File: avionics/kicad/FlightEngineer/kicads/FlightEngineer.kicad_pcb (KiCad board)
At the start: 4 copper layers, 90 x 65 mm, 67 parts

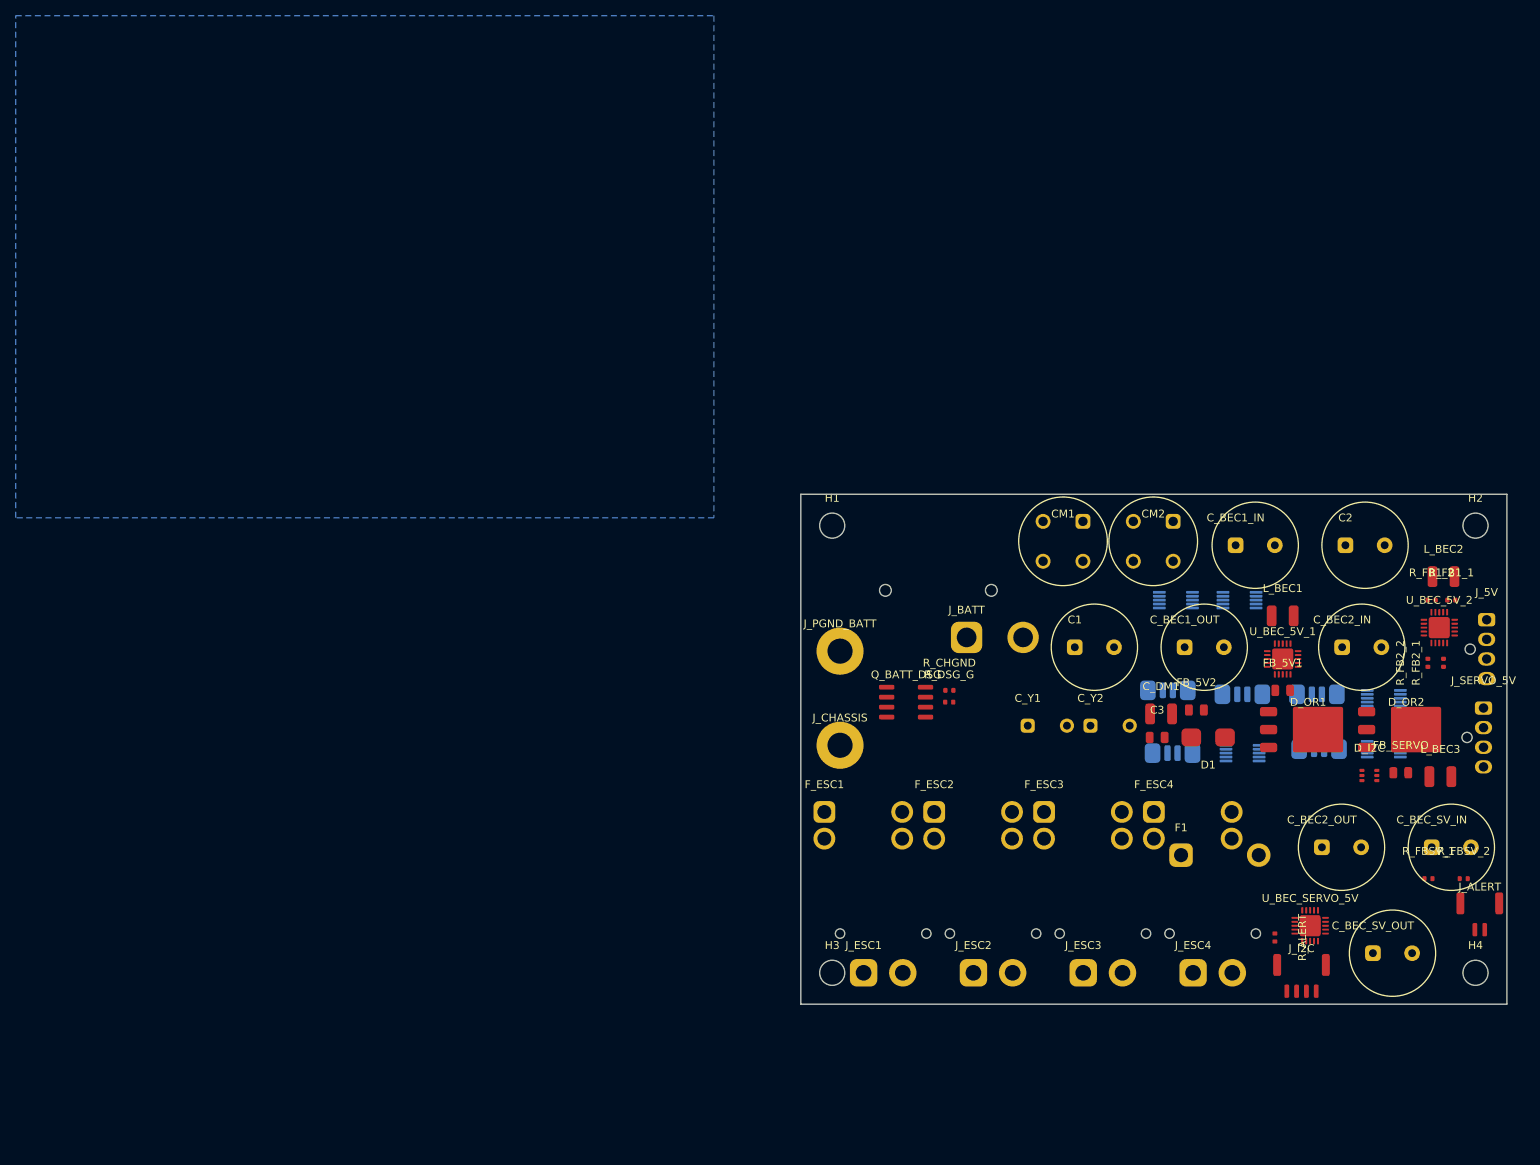
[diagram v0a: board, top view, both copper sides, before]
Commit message: feat(avionics): FlightEngineer schematic-first rebuild to ERC 0; PCB placed, DRC 31 open
Replaces FlightEngineer's legacy schematic/PCB (586 ERC violations, PCB pad
nets not matching the schematic at all, gen_flight_engineer.py itself confirmed
drifted per its own injector script's warning) with a fresh generator
pipeline matching Pilot/XO's method (gen_fe_sch.py / gen_fe_footprints.py /
gen_fe_pcb.py), transcribing every pin table from its own OEM datasheet.

Power path: TPS54620 x2 (dual-redundant diode-OR'd 5V BEC) + TPS54540 (6V
BEC), INA226 x5 (main bus + 4 ESC branches), BQ76930 6S cell monitor (Table
9-3 6-cell tap configuration). Trust module rebuilt to the CURRENT target per
FlightEngineer.md's own 2026-08-03 retarget note (MSPM0G3518-Q1 RHB-32 + real
SLB9672 + ISOW1044BDFMR + ISOW1412DFMR), not the superseded MSPM0G3507/
SLB9670 the old injector script still names; the RHB-32 pinmux is reused
verbatim from retarget_mspm0g351x_slb9672.py's own already-verified
FLIGHT_ENGINEER_REMAP/FLIGHT_ENGINEER_TPM_NETS tables rather than re-derived
from the 1500-line datasheet pin-attribute table. ISOW1412's EN/FLT pin is
now wired to a real MCU GPIO (RS485_FLT_N) instead of Pilot's hard-tied
convention, since the RHB-32 pinmux happened to free one.

One part-number defect found in FlightEngineer.md's own BOM and corrected
(flagged, not silently fixed): "AON6556" (Q_BATT_DSG, cited 60V/30A) does not
exist in AOSMD's catalog (their 30V AlphaMOS family tops out at AON6554/
6558; no 60V "6556" found) — substituted with AON6260, a real AOSMD 60V/85A
DFN5x6 MOSFET; NEEDS owner confirmation. MBRD1045CT and SMBJ33CA are
confirmed real via manufacturer/distributor catalog search but their
datasheet PDFs could not be fetched this pass (every mirror returned an HTML
block page) — standard package pinouts used, flagged for a follow-up fetch.

ERC 0 confirmed (kicad-cli sch erc --severity-all, 151 parts, 539 pins).

PCB: courtyard area was budgeted BEFORE layout per docs/solutions/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
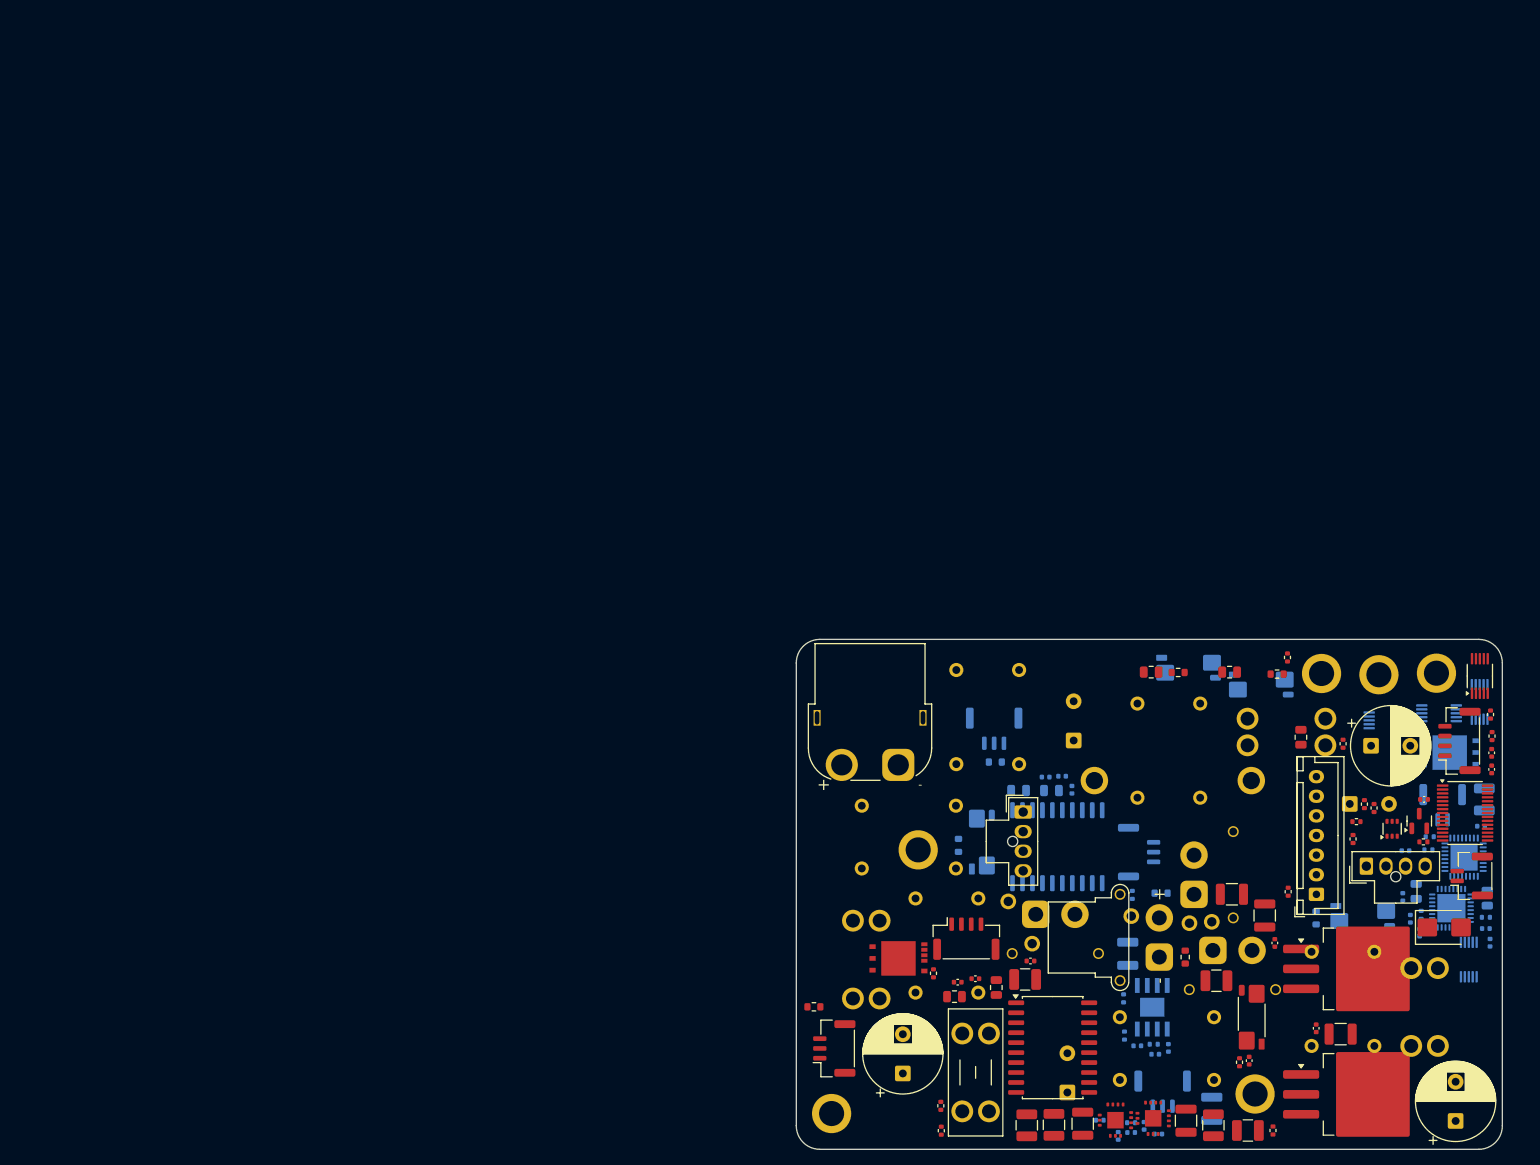
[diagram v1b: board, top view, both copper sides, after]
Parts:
- removed the C_BEC1_IN at (156.0, 68.0)
- removed C_BEC1_OUT, C_BEC2_OUT, C_BEC_SV_OUT: 100uF/50V, Capacitor_THT:CP_Radial_D10.0mm_P5.00mm
- removed the C_BEC2_IN at (169.6, 81.0)
- removed the C_BEC_SV_IN at (181.0, 106.5)
- removed FB_SERVO: WE-742792612, Capacitor_SMD:C_0805_2012Metric
- removed H1, H2, H3, H4: M3, MountingHole:MountingHole_3.2mm_M3
- removed the J_ALERT at (187.1, 115.0)
- removed the J_CHASSIS at (105.6, 93.5)
- removed the J_I2C at (164.4, 122.9)
- removed the J_PGND_BATT at (105.6, 81.5)
- removed J_SERVO_5V: NanoFit-4P_6V, Connector_Molex:Molex_Nano-Fit_105309-xx04_1x04_P2.50mm_Vertical
- removed L_BEC1, L_BEC2, L_BEC3: WE-744314100_10uH, Inductor_SMD:L_1210_3225Metric
- removed the Q_BATT_DSG at (114.0, 88.0)
- removed RS_1, RS_2, RS_3, RS_4: 1mOhm_Kelvin_2512, Flight Engineer:R_Shunt_CSS2H_2512K
- removed the RS_MAIN at (166.4, 87.0)
- removed R_FBSV_1: 100k, Resistor_SMD:R_0402_1005Metric
- removed R_FBSV_2: 30.1k, Resistor_SMD:R_0402_1005Metric
- removed U_BEC_SERVO_5V: TPS54620 sync buck 5.0V servo rail (pkg verify), Package_DFN_QFN:Texas_RGP0020D_VQFN-20-1EP_4x4mm_P0.5mm_EP2.7x2.7mm
- removed the U_IS_MAIN at (174.9, 87.5)
- added CM_ESC1: 7440640500, Serenity-Custom:Wurth_7440640500_CMC_THT, F.Cu at (147.2, 132.2)
- added CM_ESC2: 7440640500, Serenity-Custom:Wurth_7440640500_CMC_THT, B.Cu at (147.5, 94.2)
- added CM_ESC3: 7440640500, Serenity-Custom:Wurth_7440640500_CMC_THT, B.Cu at (169.7, 125.8)
- added CM_ESC4: 7440640500, Serenity-Custom:Wurth_7440640500_CMC_THT, B.Cu at (119.2, 119.0)
- added C_BEC1_BOOT: 100nF, Capacitor_SMD:C_0402_1005Metric, B.Cu at (144.3, 142.0)
- added C_BEC1_COMP: 2.2nF, Capacitor_SMD:C_0402_1005Metric, F.Cu at (157.7, 133.7)
- added C_BEC1_IN: 100uF 50V, Capacitor_SMD:C_1210_3225Metric, F.Cu at (149.7, 141.4)
- added C_BEC1_OUT1: 220uF, Capacitor_SMD:C_1210_3225Metric, F.Cu at (159.7, 115.2)
- added C_BEC1_OUT2: 100nF, Capacitor_SMD:C_0402_1005Metric, F.Cu at (161.0, 118.7)
- added C_BEC1_SS: 10nF, Capacitor_SMD:C_0402_1005Metric, B.Cu at (146.1, 143.1)
- added C_BEC2_BOOT: 100nF, Capacitor_SMD:C_0402_1005Metric, B.Cu at (138.7, 141.3)
- added C_BEC2_COMP: 2.2nF, Capacitor_SMD:C_0402_1005Metric, B.Cu at (142.7, 142.9)
- added C_BEC2_IN: 100uF 50V, Capacitor_SMD:C_1210_3225Metric, F.Cu at (136.5, 141.7)
- added C_BEC2_OUT1: 220uF, Capacitor_SMD:C_1210_3225Metric, F.Cu at (169.4, 130.3)
- added C_BEC2_OUT2: 100nF, Capacitor_SMD:C_0402_1005Metric, F.Cu at (166.3, 129.6)
- added C_BEC2_SS: 10nF, Capacitor_SMD:C_0402_1005Metric, B.Cu at (141.0, 143.3)
- added C_BEC6_BOOT: 100nF, Capacitor_SMD:C_0402_1005Metric, B.Cu at (147.4, 132.1)
- added C_BEC6_COMP: 1nF, Capacitor_SMD:C_0402_1005Metric, B.Cu at (143.5, 131.8)
- added C_BEC_SV_IN: 100uF 50V, Capacitor_SMD:C_1210_3225Metric, B.Cu at (142.2, 120.1)
- added C_BEC_SV_OUT1: 100uF, Capacitor_SMD:C_1210_3225Metric, B.Cu at (153.0, 139.8)
- added C_BEC_SV_OUT2: 100nF, Capacitor_SMD:C_0402_1005Metric, B.Cu at (145.8, 132.9)
- added C_CAP1: 0.1uF, Capacitor_SMD:C_0402_1005Metric, F.Cu at (188.6, 96.6)
- added C_CAP2: 0.1uF, Capacitor_SMD:C_0402_1005Metric, F.Cu at (180.0, 100.4)
- added C_DEC1: 470uF 35V low-ESR, Capacitor_THT:CP_Radial_D10.0mm_P5.00mm, B.Cu at (134.6, 137.8)
- added C_DEC2: 470uF 35V low-ESR, Capacitor_THT:CP_Radial_D10.0mm_P5.00mm, B.Cu at (135.4, 92.9)
- added C_DEC3: 470uF 35V low-ESR, Capacitor_THT:CP_Radial_D10.0mm_P5.00mm, F.Cu at (184.0, 141.4)
- added C_DEC4: 470uF 35V low-ESR, Capacitor_THT:CP_Radial_D10.0mm_P5.00mm, F.Cu at (113.6, 135.3)
- added C_H_IN: 10uF, Capacitor_SMD:C_0805_2012Metric, B.Cu at (188.1, 113.0)
- added C_H_OUT: 22uF, Capacitor_SMD:C_0805_2012Metric, B.Cu at (179.0, 112.1)
- added C_ISOCAN1: 10nF, Capacitor_SMD:C_0402_1005Metric, B.Cu at (135.1, 99.2)
- added C_ISOCAN2: 10uF, Capacitor_SMD:C_0805_2012Metric, B.Cu at (132.5, 99.3)
- added C_ISOCAN3: 100nF, Capacitor_SMD:C_0402_1005Metric, B.Cu at (131.8, 97.6)
- added C_ISOCAN4: 10nF, Capacitor_SMD:C_0402_1005Metric, B.Cu at (133.9, 97.4)
- added C_ISOCAN5: 10uF, Capacitor_SMD:C_0805_2012Metric, B.Cu at (128.3, 99.3)
- added C_MCU_3V3: 100nF, Capacitor_SMD:C_0402_1005Metric, B.Cu at (187.3, 103.8)
- added C_MCU_VCORE: 1uF, Capacitor_SMD:C_0402_1005Metric, B.Cu at (177.3, 112.8)
- added C_NTC: 100nF X7R, Capacitor_SMD:C_0402_1005Metric, B.Cu at (177.7, 106.9)
- added C_REGOUT: 1uF, Capacitor_SMD:C_0402_1005Metric, F.Cu at (188.6, 94.5)
- added C_RS485_1: 10nF, Capacitor_SMD:C_0402_1005Metric, F.Cu at (129.8, 121.0)
- added C_RS485_2: 10uF, Capacitor_SMD:C_0805_2012Metric, F.Cu at (125.5, 124.4)
- added C_RS485_3: 100nF, Capacitor_SMD:C_0402_1005Metric, F.Cu at (122.8, 123.3)
- added C_RS485_4: 10nF, Capacitor_SMD:C_0402_1005Metric, F.Cu at (120.6, 123.7)
- added C_RS485_5: 10uF, Capacitor_SMD:C_0805_2012Metric, F.Cu at (120.2, 125.5)
- added C_TPM1: 1uF, Capacitor_SMD:C_0402_1005Metric, B.Cu at (187.9, 116.9)
- added C_TPM2: 100nF, Capacitor_SMD:C_0402_1005Metric, B.Cu at (179.5, 117.4)
- added C_TPM3: 100nF, Capacitor_SMD:C_0402_1005Metric, B.Cu at (178.3, 115.6)
- added C_TPM4: 100nF, Capacitor_SMD:C_0402_1005Metric, B.Cu at (188.4, 118.7)
- added ESC1_LINK: 0R link, Resistor_SMD:R_0603_1608Metric, F.Cu at (149.6, 120.5)
- added ESC2_LINK: 0R link, Resistor_SMD:R_0603_1608Metric, B.Cu at (146.5, 112.3)
- added ESC3_LINK: 0R link, Resistor_SMD:R_0603_1608Metric, B.Cu at (166.3, 115.5)
- added ESC4_LINK: 0R link, Resistor_SMD:R_0603_1608Metric, B.Cu at (120.7, 106.3)
- added FB_6V: 742792612, Inductor_SMD:L_1210_3225Metric, F.Cu at (129.2, 123.4)
- added J_485_IN: SM03B-GHS-TB, Connector_JST:JST_GH_SM03B-GHS-TB_1x03-1MP_P1.25mm_Horizontal, B.Cu at (146.7, 137.7)
- added J_485_OUT: SM03B-GHS-TB, Connector_JST:JST_GH_SM03B-GHS-TB_1x03-1MP_P1.25mm_Horizontal, F.Cu at (104.8, 132.1)
- added J_6V: Nano-Fit 4P, Connector_Molex:Molex_Nano-Fit_105309-xx04_1x04_P2.50mm_Vertical, F.Cu at (172.7, 108.9)
- added J_ALERT: SM02B-GHS-TB, Connector_JST:JST_GH_SM02B-GHS-TB_1x02-1MP_P1.25mm_Horizontal, F.Cu at (186.1, 110.2)
- added J_BAL: XH-7P, Connector_JST:JST_XH_B7B-XH-A_1x07_P2.50mm_Vertical, F.Cu at (166.3, 112.5)
- added J_CAN_IN: SM03B-GHS-TB, Connector_JST:JST_GH_SM03B-GHS-TB_1x03-1MP_P1.25mm_Horizontal, B.Cu at (143.7, 107.1)
- added J_CAN_OUT: SM03B-GHS-TB, Connector_JST:JST_GH_SM03B-GHS-TB_1x03-1MP_P1.25mm_Horizontal, B.Cu at (125.2, 91.4)
- added J_CHASSIS: M3 standoff x4, Serenity-Custom:M3_Chassis_Lug_PGND, F.Cu at (167.0, 84.3)
- added J_I2C: SM04B-GHS-TB, Connector_JST:JST_GH_SM04B-GHS-TB_1x04-1MP_P1.25mm_Horizontal, F.Cu at (184.5, 92.9)
- added J_NTC: SM02B-GHS-TB, Connector_JST:JST_GH_SM02B-GHS-TB_1x02-1MP_P1.25mm_Horizontal, B.Cu at (182.4, 101.1)
- added J_PGND_BATT: M3 chassis lug, Serenity-Custom:M3_Chassis_Lug_PGND, F.Cu at (174.3, 84.5)
- added J_SHLD_5V: PGND via, Serenity-Custom:PGND_ViaPad_1p2mm, F.Cu at (150.1, 116.2)
- added J_SHLD_6V: PGND via, Serenity-Custom:PGND_ViaPad_1p2mm, F.Cu at (153.0, 116.0)
- added J_SHLD_ALERT: PGND via, Serenity-Custom:PGND_ViaPad_1p2mm, B.Cu at (142.7, 115.3)
- added J_SHLD_ESC1: M3 chassis lug, Serenity-Custom:M3_Chassis_Lug_PGND, F.Cu at (181.6, 84.3)
- added J_SHLD_ESC2: M3 chassis lug, Serenity-Custom:M3_Chassis_Lug_PGND, F.Cu at (104.5, 140.4)
- added J_SHLD_ESC3: M3 chassis lug, Serenity-Custom:M3_Chassis_Lug_PGND, B.Cu at (158.5, 137.9)
- added J_SHLD_ESC4: M3 chassis lug, Serenity-Custom:M3_Chassis_Lug_PGND, B.Cu at (115.5, 106.8)
- added J_SHLD_I2C: PGND via, Serenity-Custom:PGND_ViaPad_1p2mm, F.Cu at (130.1, 118.8)
- added J_SHLD_NTC: PGND via, Serenity-Custom:PGND_ViaPad_1p2mm, F.Cu at (127.0, 113.4)
- added J_SWD_H: SM04B-GHS-TB, Connector_JST:JST_GH_SM04B-GHS-TB_1x04-1MP_P1.25mm_Horizontal, F.Cu at (121.7, 118.2)
- added L1: 10uH 6A, Inductor_SMD:L_1210_3225Metric, F.Cu at (157.6, 142.6)
- added L2: 10uH 6A, Inductor_SMD:L_1210_3225Metric, F.Cu at (129.4, 141.9)
- added L3: 10uH 6A, Inductor_SMD:L_1210_3225Metric, F.Cu at (153.6, 123.5)
- added L_H1: 2.2uH, Inductor_SMD:L_1210_3225Metric, B.Cu at (187.7, 100.4)
- added Q_BATT_CHG: AON6260 (DNP), Serenity-Custom:AOSMD_DFN5x6-8L, B.Cu at (183.3, 94.4)
- added Q_BATT_DSG: AON6260, Serenity-Custom:AOSMD_DFN5x6-8L, F.Cu at (113.0, 120.7)
- added RS1: 1mOhm 3W Kelvin, Resistor_SMD:R_Shunt_Vishay_WSK2512_6332Metric_T1.19mm, F.Cu at (158.0, 128.2)
- added RS2: 1mOhm 3W Kelvin, Resistor_SMD:R_Shunt_Vishay_WSK2512_6332Metric_T1.19mm, B.Cu at (150.0, 83.6)
- added RS3: 1mOhm 3W Kelvin, Resistor_SMD:R_Shunt_Vishay_WSK2512_6332Metric_T1.19mm, B.Cu at (172.2, 115.3)
- added RS4: 1mOhm 3W Kelvin, Resistor_SMD:R_Shunt_Vishay_WSK2512_6332Metric_T1.19mm, B.Cu at (123.7, 105.8)
- added RS_MAIN: 1mOhm 5W Kelvin, Resistor_SMD:R_Shunt_Vishay_WSK2512_6332Metric_T1.19mm, B.Cu at (159.3, 85.8)
- added R_485TERM: 120R, Resistor_SMD:R_0603_1608Metric, F.Cu at (102.2, 126.8)
- added R_BAL1: 100R, Resistor_SMD:R_0402_1005Metric, F.Cu at (162.7, 112.2)
- added R_BAL2: 100R, Resistor_SMD:R_0402_1005Metric, F.Cu at (171.0, 105.4)
- added R_BAL3: 100R, Resistor_SMD:R_0402_1005Metric, F.Cu at (171.4, 103.2)
- added R_BAL4: 100R, Resistor_SMD:R_0402_1005Metric, F.Cu at (172.4, 101.0)
- added R_BAL5: 100R, Resistor_SMD:R_0402_1005Metric, F.Cu at (173.7, 101.5)
- added R_BAL6: 100R, Resistor_SMD:R_0402_1005Metric, F.Cu at (169.7, 93.3)
- added R_CANSTB: 0R, Resistor_SMD:R_0402_1005Metric, B.Cu at (142.8, 112.6)
- added R_CANTERM: 120R, Resistor_SMD:R_0603_1608Metric, B.Cu at (125.4, 95.6)
- added R_EN_BIAS: 100k, Resistor_SMD:R_0402_1005Metric, B.Cu at (145.6, 131.6)
- added R_FB6_1: 64.9k 1%, Resistor_SMD:R_0402_1005Metric, B.Cu at (141.7, 125.8)
- added R_FB6_2: 10.0k 1%, Resistor_SMD:R_0402_1005Metric, B.Cu at (141.8, 130.5)
- added R_GND_PGND: 0R, Resistor_SMD:R_0603_1608Metric, F.Cu at (148.7, 84.2)
- added R_I2C_SCL: 4.7k, Resistor_SMD:R_0402_1005Metric, F.Cu at (188.7, 92.3)
- added R_I2C_SDA: 4.7k, Resistor_SMD:R_0402_1005Metric, F.Cu at (188.5, 89.6)
- added R_MCU_NRST: 10k, Resistor_SMD:R_0402_1005Metric, B.Cu at (180.6, 106.8)
- added R_NTC_PU: 10k, Resistor_SMD:R_0402_1005Metric, B.Cu at (180.7, 105.2)
- added R_RS485FLT_PU: 10k, Resistor_SMD:R_0402_1005Metric, F.Cu at (118.4, 139.5)
- added R_TPM10: 10k, Resistor_SMD:R_0402_1005Metric, B.Cu at (179.7, 115.1)
- added R_TPMCS: 10k, Resistor_SMD:R_0402_1005Metric, B.Cu at (187.9, 115.4)
- added U_BEC_6V: TPS54540DDAR, Package_SO:TI_SO-PowerPAD-8, B.Cu at (145.4, 126.9)
- added U_CELL: BQ76930PWRQ1, Package_SO:TSSOP-30_4.4x7.8mm_P0.5mm, F.Cu at (185.3, 102.1)
- added U_ISOCAN: ISOW1044BDFMR, Package_SO:SOIC-20W_7.5x12.8mm_P1.27mm, B.Cu at (133.3, 106.4)
- added U_IS_MAIN: INA226AIDGSR, Package_SO:VSSOP-10_3x3mm_P0.5mm, B.Cu at (185.7, 120.8)
- added U_MCU: MSPM0G3518-Q1, Package_DFN_QFN:Texas_RHB0032E_VQFN-32-1EP_5x5mm_P0.5mm_EP3.45x3.45mm, B.Cu at (185.1, 107.8)
- added U_REG_3V3_H: TLV62569DBVR, Package_TO_SOT_SMD:SOT-23, F.Cu at (179.4, 103.2)
- added U_RS485: ISOW1412DFMR, Package_SO:SOIC-20W_7.5x12.8mm_P1.27mm, F.Cu at (132.7, 132.0)
- added U_TPM: SLB9672XU20, Package_DFN_QFN:QFN-32-1EP_5x5mm_P0.5mm_EP3.6x3.6mm, B.Cu at (183.5, 114.3)
- added VDIS_LINK: 0R link, Resistor_SMD:R_0603_1608Metric, F.Cu at (161.3, 84.4)
- C1: value 220uF/35V -> 220uF 35V; moved to B.Cu
- C2: value 220uF/35V -> 220uF 35V
- C3: value 100nF/50V -> 100nF X7R 0805
- CM1, CM2: value WE-SL5_7440640500 -> 7440640500; footprint Flight Engineer:CMC_WE-SL5_7440640500 -> Serenity-Custom:Wurth_7440640500_CMC_THT
- C_DM1: value 10uF/50V -> 10uF 50V X7R 1210; footprint Inductor_SMD:L_1210_3225Metric -> Capacitor_SMD:C_1210_3225Metric
- C_Y1, C_Y2: value 4.7nF/250V_Y2 -> 4.7nF 250V Y2; footprint Capacitor_THT:C_Disc_D4.3mm_W1.9mm_P5.00mm -> Capacitor_SMD:C_0805_2012Metric
- D_OR1, D_OR2: footprint Package_TO_SOT_SMD:TO-252-3_TabPin2 -> Package_TO_SOT_SMD:TO-263-3_TabPin2
- F1: value FuseHolder_MAXI_150A -> 0297150.ZXNV 150A MAXI; footprint Flight Engineer:FuseHolder_MAXI_PCB -> Serenity-Custom:MAXI_Blade_Fuseholder_2P
- FB_5V1, FB_5V2: value WE-742792612 -> 742792612; footprint Capacitor_SMD:C_0805_2012Metric -> Inductor_SMD:L_1210_3225Metric
- F_ESC1: value FuseHolder_Mini_40A -> 0297040.WXNV 40A mini
- F_ESC2, F_ESC3, F_ESC4: value FuseHolder_Mini_40A -> 0297040.WXNV 40A mini; moved to B.Cu
- J_5V: value NanoFit-4P_5V -> Nano-Fit 4P
- J_ESC1: value XT30PW-F_ESC1 -> XT30PW-F
- J_ESC2: value XT30PW-F_ESC2 -> XT30PW-F; moved to B.Cu
- J_ESC3: value XT30PW-F_ESC3 -> XT30PW-F; moved to B.Cu
- J_ESC4: value XT30PW-F_ESC4 -> XT30PW-F; moved to B.Cu
- R_CHGND: value 0R -> 0R socketed
- R_FB1_1, R_FB2_1: value 100k -> 56.2k 1%
- R_FB1_2: value 22.1k -> 10.0k 1%
- R_FB2_2: value 22.1k -> 10.0k 1%; moved to B.Cu
- U_BEC_5V_1, U_BEC_5V_2: footprint Package_DFN_QFN:Texas_RGP0020D_VQFN-20-1EP_4x4mm_P0.5mm_EP2.7x2.7mm -> Serenity-Custom:Texas_RGY0014A_VQFN-14-1EP_3.5x3.5mm
- U_IS1: value INA226_0x40 -> INA226AIDGSR; footprint Package_SO:MSOP-10_3x3mm_P0.5mm -> Package_SO:VSSOP-10_3x3mm_P0.5mm; moved to F.Cu
- U_IS2: value INA226_0x41 -> INA226AIDGSR; footprint Package_SO:MSOP-10_3x3mm_P0.5mm -> Package_SO:VSSOP-10_3x3mm_P0.5mm
- U_IS3: value INA226_0x42 -> INA226AIDGSR; footprint Package_SO:MSOP-10_3x3mm_P0.5mm -> Package_SO:VSSOP-10_3x3mm_P0.5mm
- U_IS4: value INA226_0x43 -> INA226AIDGSR; footprint Package_SO:MSOP-10_3x3mm_P0.5mm -> Package_SO:VSSOP-10_3x3mm_P0.5mm
- moved R_FB2_1 87.5 mm to (118.5, 142.6)
- moved U_BEC_5V_2 75.1 mm to (140.7, 141.3)
- moved R_FB1_1 71.3 mm to (160.8, 142.6), turned to 90 degrees
- moved R_FB2_2 69.8 mm to (142.7, 141.6), turned to 0 degrees
- moved J_5V 64.0 mm to (128.9, 102.0)
- moved R_FB1_2 63.8 mm to (156.5, 133.9), turned to 90 degrees
- moved U_BEC_5V_1 60.8 mm to (145.5, 141.1)
- moved F_ESC3 58.4 mm to (181.8, 131.8), turned to 90 degrees
- moved FB_5V1 56.1 mm to (153.2, 141.9), turned to 90 degrees
- moved FB_5V2 55.9 mm to (132.8, 141.9), turned to 90 degrees
- moved D_OR2 46.9 mm to (172.0, 138.0)
- moved R_CHGND 43.3 mm to (162.6, 82.3), turned to 90 degrees
- moved CM1 42.5 mm to (114.4, 105.2)
- moved F_ESC4 42.3 mm to (110.6, 125.8), turned to 90 degrees
- moved F_ESC1 42.0 mm to (121.2, 140.2), turned to 90 degrees
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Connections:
- C1 pad 1: VDIS -> VBAT_F1
- C2 pad 1: VDIS -> VBAT_F1
- C3 pad 1: VDIS -> VBAT_F1
- CM1 pad 1: VDIS -> BATT_RAW_P
- CM1 pad 2: VDIS -> BATT_CM1_P
- CM1 pad 3: PGND -> BATT_RAW_N
- CM1 pad 4: PGND -> BATT_CM1_N
- CM2 pad 1: VDIS -> BATT_CM1_P
- CM2 pad 2: VDIS -> VBAT
- CM2 pad 3: PGND -> BATT_CM1_N
- C_DM1 pad 1: VDIS -> VBAT_F1
- C_Y1 pad 1: VDIS -> VBAT_F1
- C_Y1 pad 2: CHASSIS -> J_CHASSIS_NET
- C_Y2 pad 2: CHASSIS -> J_CHASSIS_NET
- D1 pad 1: PGND -> VBAT_F1
- D1 pad 2: VDIS -> PGND
- D_I2C pad 1: PGND -> I2C_SCL
- D_I2C pad 2: PDB_SDA_RAW -> PGND
- D_I2C pad 3: PDB_SCL_RAW -> I2C_SDA
- D_I2C pad 4: PDB_SCL -> (no net)
- D_I2C pad 5: PDB_SDA -> +5V
- D_I2C pad 6: +5V -> (no net)
- D_OR1 pad 1: BEC1_PRE_OR -> +5V_PRE_OR1
- D_OR1 pad 2: +5V -> +5V_AVIONICS
- D_OR1 pad 3: BEC2_PRE_OR -> +5V_AVIONICS
- D_OR2 pad 1: BEC2_PRE_OR -> +5V_PRE_OR2
- D_OR2 pad 2: +5V -> +5V_AVIONICS
- D_OR2 pad 3: BEC2_PRE_OR -> +5V_AVIONICS
- F1 pad 1: VDIS -> VBAT
- F1 pad 2: VDIS -> VBAT_F1
- FB_5V1 pad 2: BEC1_VIN_F -> VDIS_5V1
- FB_5V2 pad 2: BEC2_VIN_F -> VDIS_5V2
- F_ESC1 pad 1: VBAT -> VDIS
- F_ESC2 pad 1: VBAT -> VDIS
- F_ESC3 pad 1: VBAT -> VDIS
- F_ESC4 pad 1: VBAT -> VDIS
- J_5V pad 1: PGND -> +5V_AVIONICS
- J_5V pad 2: PGND -> +5V_AVIONICS
- J_5V pad 3: +5V -> GND
- J_5V pad 4: +5V -> GND
- J_BATT pad 1: VDIS -> BATT_RAW_P
- J_BATT pad 2: PGND -> BATT_RAW_N
- J_ESC1 pad 1: ESC1_RS_OUT -> ESC1_OUT
- J_ESC2 pad 1: ESC2_RS_OUT -> ESC2_OUT
- J_ESC3 pad 1: ESC3_RS_OUT -> ESC3_OUT
- J_ESC4 pad 1: ESC4_RS_OUT -> ESC4_OUT
- R_ALERT pad 2: PDB_ALERT_N -> CELL_ALERT_N
- R_CHGND pad 1: PGND -> J_CHASSIS_NET
- R_CHGND pad 2: CHASSIS -> PGND
- R_DSG_G pad 1: DSG_GATE -> BATT_DSG_GATE
- R_DSG_G pad 2: PGND -> BATT_DSG_GATE_R
- R_FB1_1 pad 1: BEC1_PRE_OR -> +5V_PRE_OR1
- R_FB1_2 pad 2: PGND -> GND
- R_FB2_1 pad 1: BEC2_PRE_OR -> +5V_PRE_OR2
- R_FB2_2 pad 2: PGND -> GND
- U_BEC_5V_1 pad 1: BEC1_VIN_F -> GND
- U_BEC_5V_1 pad 10: PGND -> +3V3_BIAS_EN
- U_BEC_5V_1 pad 11: BEC1_PRE_OR -> BEC1_SW
- U_BEC_5V_1 pad 12: (no net) -> BEC1_SW
- U_BEC_5V_1 pad 13: (no net) -> BEC1_BOOT
- U_BEC_5V_1 pad 15: BEC1_VIN_F -> GND
- U_BEC_5V_1 pad 2: (no net) -> GND
- U_BEC_5V_1 pad 3: (no net) -> GND
- U_BEC_5V_1 pad 4: (no net) -> VDIS
- U_BEC_5V_1 pad 5: BEC1_SW -> VDIS
- U_BEC_5V_1 pad 6: BEC1_SW -> VDIS
- U_BEC_5V_1 pad 7: PGND -> BEC1_FB
- U_BEC_5V_1 pad 8: PGND -> BEC1_COMP
- U_BEC_5V_1 pad 9: PGND -> BEC1_SS
- U_BEC_5V_2 pad 1: BEC2_VIN_F -> GND
- U_BEC_5V_2 pad 10: PGND -> +3V3_BIAS_EN
- U_BEC_5V_2 pad 11: BEC2_PRE_OR -> BEC2_SW
- U_BEC_5V_2 pad 12: (no net) -> BEC2_SW
- U_BEC_5V_2 pad 13: (no net) -> BEC2_BOOT
- U_BEC_5V_2 pad 15: BEC2_VIN_F -> GND
- U_BEC_5V_2 pad 2: (no net) -> GND
- U_BEC_5V_2 pad 3: (no net) -> GND
- U_BEC_5V_2 pad 4: (no net) -> VDIS
- U_BEC_5V_2 pad 5: BEC2_SW -> VDIS
- U_BEC_5V_2 pad 6: BEC2_SW -> VDIS
- U_BEC_5V_2 pad 7: PGND -> BEC2_FB
- U_BEC_5V_2 pad 8: PGND -> BEC2_COMP
- U_BEC_5V_2 pad 9: PGND -> BEC2_SS
- U_IS1 pad 1: ESC1_SNS_P -> GND
- U_IS1 pad 10: ESC1_FUSED -> SHUNT1_P
- U_IS1 pad 2: ESC1_SNS_N -> GND
- U_IS1 pad 3: PGND -> (no net)
- U_IS1 pad 4: +5V -> I2C_SDA
- U_IS1 pad 5: PDB_SDA -> I2C_SCL
- U_IS1 pad 6: PDB_SCL -> +5V
- U_IS1 pad 7: PDB_ALERT_N -> GND
- U_IS1 pad 8: (no net) -> VDIS
- U_IS1 pad 9: (no net) -> SHUNT1_N
- U_IS2 pad 1: ESC2_SNS_P -> GND
- U_IS2 pad 10: ESC2_FUSED -> SHUNT2_P
- U_IS2 pad 2: ESC2_SNS_N -> +5V
- U_IS2 pad 3: PGND -> (no net)
- U_IS2 pad 4: +5V -> I2C_SDA
- U_IS2 pad 5: PDB_SDA -> I2C_SCL
- U_IS2 pad 6: PDB_SCL -> +5V
- U_IS2 pad 7: PDB_ALERT_N -> GND
- U_IS2 pad 8: (no net) -> VDIS
- U_IS2 pad 9: (no net) -> SHUNT2_N
- U_IS3 pad 1: ESC3_SNS_P -> GND
- U_IS3 pad 10: ESC3_FUSED -> SHUNT3_P
- U_IS3 pad 2: ESC3_SNS_N -> I2C_SDA
- U_IS3 pad 3: PGND -> (no net)
- U_IS3 pad 4: +5V -> I2C_SDA
- U_IS3 pad 5: PDB_SDA -> I2C_SCL
- U_IS3 pad 6: PDB_SCL -> +5V
- U_IS3 pad 7: PDB_ALERT_N -> GND
- U_IS3 pad 8: (no net) -> VDIS
- U_IS3 pad 9: (no net) -> SHUNT3_N
- U_IS4 pad 1: ESC4_SNS_P -> GND
- U_IS4 pad 10: ESC4_FUSED -> SHUNT4_P
- U_IS4 pad 2: ESC4_SNS_N -> I2C_SCL
- U_IS4 pad 3: PGND -> (no net)
- U_IS4 pad 4: +5V -> I2C_SDA
- U_IS4 pad 5: PDB_SDA -> I2C_SCL
- U_IS4 pad 6: PDB_SCL -> +5V
- U_IS4 pad 7: PDB_ALERT_N -> GND
- U_IS4 pad 8: (no net) -> VDIS
- U_IS4 pad 9: (no net) -> SHUNT4_N
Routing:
- added copper zone on In1.Cu, net GND
- added copper zone on In2.Cu, net VBAT
- removed copper zone on In1.Cu, net PGND
- removed copper zone on B.Cu, net VBAT
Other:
- outline, holes or cut-outs redrawn
- board text added: "FLIGHT ENGINEER Rev R2 Griffing Technology LLC CC BY 4.0"
- board text removed: "Flight Engineer Rev R"
- board text removed: "Griffing Technology LLC | CC BY 4.0"

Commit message: docs(avionics): Wurth usage notice + uncrewed-only statement on 5 boards; catalogue REF-SENSOR-022..040
Owner decision 2026-09-26: retain the Wurth parts. The Wurth datasheet
usage notice is quoted verbatim [REF-SENSOR-028: Wurth 749010012A data
sheet rev 004.000 p.1] with an 'intended for use only on uncrewed
aircraft' statement in each Wurth-bearing board's .md, as a schematic
text item and PCB Cmts.User text, and in title-block comments 8/9
(tools/add_board_notices.py, idempotent). ERC/DRC/parity counts
unchanged on all five boards (kicad-cli 9.0.2).

REFERENCES.md: REF-SENSOR-022/023/025-030/033/038/040 were cited by
board schematics and generator scripts but never catalogued; entries
added with URLs validated 2026-09-26, unreachable ones marked
'requires verification'.

AI-authored: Claude Opus 5.5 (Anthropic).

Co-Authored-By: Claude Opus 5.5 <noreply@anthropic.com>
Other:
- board text added: "WÜRTH ELEKTRONIK USAGE NOTICE (verbatim, 749010012A data sheet rev 004.000 p.1; applies to Würth parts on this board: 7440640500, 742792612): This electronic component has been designed and developed for usage in general electronic equipment only. This product is not authorized for use in equipment where a higher safety standard and reliability standard is especially required or where a failure o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"
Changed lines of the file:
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@@
 		(comment 1 "Power/monitoring node, 90 x 65 mm, 4-layer; generated by gen_fe_pcb.py")
 		(comment 2 "Author: Claude Sonnet 5 (2026-09-20); owner sgriffing; CC BY 4.0")
+		(comment 8 "Wurth parts (7440640500, 742792612): see Wurth usage notice on this page [USAGE-NOTICE-2026-09-26]")
+		(comment 9 "Intended for use ONLY on uncrewed aircraft")
 	)
 	(layers
@@
 	)
 	(embedded_fonts no)
+	(gr_text "WÜRTH ELEKTRONIK USAGE NOTICE (verbatim, 749010012A data sheet rev 004.000 p.1; applies to Würth\nparts on this board: 7440640500, 742792612):\n\nThis electronic component has been designed and developed for usage in general electronic equipment\nonly. This product is not authorized for use in equipment where a higher safety standard and\nreliability standard is especially required or where a failure of the product is reasonably expected\nto cause severe personal injury or death, unless the parties have executed an agreement specifically\ngoverning such use. Moreover Würth Elektronik eiSos GmbH & Co KG products are neither designed nor\nintended for use in areas such as military, aerospace, aviation, nuclear control, submarine,\ntransportation, transportation signal, disaster prevention, medical, public information network\netc.. Würth Elektronik eiSos GmbH & Co KG must be informed about the intent of such usage before the\ndesign-in stage. In addition, sufficient reliability evaluation checks for safety must be performed\non every electronic component which is used in electrical circuits that require high safety and\nreliability functions or performance.\n\nINTENDED USE: The Serenity-UAV avionics, including this board, are intended for use only on uncrewed\naircraft.\n[USAGE-NOTICE-2026-09-26]"
+		(at 195.00 80.00 0)
+		(layer "Cmts.User")
+		(effects (font (size 0.8 0.8) (thickness 0.1)) (justify left top))
+	)
 )

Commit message: fix(avionics): TLV62569 -> TLV62569PDRLR and TLV75725 -> TLV75725PDRVR package swaps; regulator circuit fixes; stale-component cleanup
Owner-approved swaps (2026-09-26, avionics/WBS.md U7.1e) using the
datasheet-verified SecureControllers library via ${SECURE_CONTROLLERS_LIB}:
- CAN-PERIPH-GW-1 U_REG_3V3, Observer U_REG_3V3/U_REG_1V2, Flight
  Engineer U_REG_3V3_H -> TLV62569PDRLR (SOT-563, 1.6 x 1.6 mm).
  Pins remapped by name; the old symbols had FB/PG swapped (gateway,
  Observer) or sat on a 3-pad SOT-23 (Flight Engineer).
- Observer U_REG_2V5 -> TLV75725PDRVR (WSON-6 2x2, EP to GND).
- Feedback dividers per TLV62569 Sec. 8.2.2.2 Eq. 2 (VFB 0.6 V):
  gateway 10k/20k (0.9 V!) -> 453k/100k = 3.318 V; Observer placeholders
  -> 453k/100k (3V3) and 100k/100k (1V2).
- Flight Engineer: EN was tied to its own 3V3 output and FB straight to
  +3V3 (would regulate at 0.6 V); EN -> +5V, added R_H_FBT 453k /
  R_H_FBB 100k. Parity 2 -> 0, ERC 0.
- tools/kicad_prune_stale.py: parity-driven removal of stale electrical
  footprints and only the copper they orphan; mounting holes are marked
  board_only + renumbered (Commo parity 93 -> 86, Observer 21 -> 17).
- New tools kicad_relink.py / kicad_add_part.py / kicad_set_value.py;
  SecureControllers entries added to every board's lib tables.

Sources: TI TLV62569 (SLVSDG1C) Pin Functions, Sec. 8.2.2.2; TI TLV757P
Fig. 4-3, Pin Functions, DRV0006A.

AI-authored: Claude Opus 5.5 (Anthropic).

Co-Authored-By: Claude Opus 5.5 <noreply@anthropic.com>
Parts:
- added R_H_FBB: 100k 1%, Resistor_SMD:R_0402_1005Metric, F.Cu at (177.6, 99.9)
- added R_H_FBT: 453k 1%, Resistor_SMD:R_0402_1005Metric, F.Cu at (177.6, 101.6)
- U_REG_3V3_H: value TLV62569DBVR -> TLV62569PDRLR; footprint Package_TO_SOT_SMD:SOT-23 -> Package_TO_SOT_SMD:SOT-563
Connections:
- U_REG_3V3_H pad 1: +3V3 -> REG3V3_FB
- U_REG_3V3_H pad 3: REG3V3_SW -> +5V

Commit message: fix(avionics): PRTR5V0U2X package/pinout fix on all 12 instances, 5 boards
Owner-approved 2026-09-26 (avionics/WBS.md U7.2). Per Nexperia
PRTR5V0U2X datasheet Table 2 (SOT143B: 1=GND, 2=I/O1, 3=I/O2, 4=VCC),
relinked via tools/kicad_relink.py --rewire (same footprint position/
rotation preserved, only package + pin-to-net correspondence corrected):

- Pilot TVS-CAN, TVS-RS485; TACCO TVS-CAN, TVS-RS485; FlightEngineer
  D_I2C: straightforward SOT-363->SOT-143 swap with existing GND/VCC
  nets carried over unchanged (5 instances).
- Observer T1_D1/T1_D2/T2_D1/T2_D2 (Ethernet magnetics ESD) and D5
  (CAN-FD), Commo 'ANT TVS' and 'UART TVS': these had no VCC net at
  all in the original (wrong-package) design -- VCC tied to the local
  GND/PGND net as a conservative fallback (line-to-line and
  line-to-ground clamping preserved; the rail-clamp direction is
  inert). This is a judgment call, not a datasheet requirement --
  flagged for review, not a silent assumption (7 instances).

ERC unchanged (0/0/0/0/154-pre-existing) on all 5 boards; DRC/parity
flat or improved except one new courtyard-overlap warning on Pilot
(TVS-CAN vs C-IN1, mechanical only) left unresolved rather than guess
a nudge direction without full layout context.

AI-authored: Claude Sonnet 5 (Anthropic).

Co-Authored-By: Claude Sonnet 5 <noreply@anthropic.com>
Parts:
- D_I2C: footprint Package_TO_SOT_SMD:SOT-363_SC-70-6 -> Package_TO_SOT_SMD:SOT-143
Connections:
- D_I2C pad 1: I2C_SCL -> PGND
- D_I2C pad 2: PGND -> I2C_SCL
- D_I2C pad 4: (no net) -> +5V
